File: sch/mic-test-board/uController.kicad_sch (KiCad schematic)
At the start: 3 parts, among them U34 SN74LVC126ARGYR, U5 NUCLEO144-H743ZI

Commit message: pcb: commit before large routing effort
 - schematic refactor to split preamps to each mic board
 - Mic board and main board are placed
 - no tracks laid
 - critical parts selected
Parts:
- added J1: CN11.female, ~, symbol Connector_Generic:Conn_02x35_Odd_Even
- added J5: CN12.female, ~, symbol Connector_Generic:Conn_02x35_Odd_Even
- added J6: CN11.male, ~, symbol Connector_Generic:Conn_02x35_Odd_Even
- added JP10, JP11, JP12, JP13, JP14, JP15, JP16, JP17, JP20, JP21, JP3, JP4, JP5, JP6, JP7, JP8, JP9: SolderJumper_2_Bridged, Jumper:SolderJumper-2_P1.3mm_Bridged_Pad1.0x1.5mm, symbol Jumper:SolderJumper_2_Bridged
- added R118, R119, R120: 0R, Resistor_SMD:R_0603_1608Metric, symbol Device:R_Small
- added R50, R52: 49.9k, Resistor_SMD:R_0603_1608Metric, symbol Device:R_Small
- added TP23, TP24, TP25, TP26, TP27, TP28, TP29, TP30, TP31, TP32, TP33, TP34, TP35: TestPoint, TestPoint:TestPoint_Pad_D1.0mm, symbol Connector:TestPoint
- C201: footprint (none) -> Capacitor_SMD:C_0603_1608Metric
- U5: footprint Module:ST_Morpho_Connector_144_STLink -> mic-test-board:ST_Morpho_Connector_144_STLink_SMD_Headers_BottomMount
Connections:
- net +3.3V: now also JP11.1 (A), JP12.1 (A), R50.2, R52.2
- net GND: now also U34.13
- net GPIO_DRDY: now also U5.140 (PG5), JP13.1 (A), TP27.1; no longer U34.1
- net GPIO_~{START}: now also JP14.1 (A), TP30.1
- net SPI1_MISO: now also JP21.1 (A), TP35.1
- net SPI1_MOSI: now also JP20.1 (A), TP34.1
- net SPI1_SCLK: now also JP17.1 (A), TP33.1
- net SPI1_~{CS1}: now also JP15.1 (A), TP31.1
- net SPI1_~{CS2}: now also JP16.1 (A), TP32.1
- net SPI2_MOSI1: now also TP28.1
- net SPI2_MOSI2: now also TP29.1
- net SPI2_SCLK: now also TP26.1
- net V_{IN}: now also U5.24 (VIN)
- net at U34.4: now also JP11.2 (B)
- net at U34.6: now also R119.1, TP24.1
- net SPI2_SCLK_buff: now reaches U5.114 (PF10)
- net SPI2_SCLK_buff: now also R118.2
- net GPIO_~{START}_uC: now reaches U5.141 (PG4)
- net GPIO_~{START}_uC: now also JP14.2 (B)
- net SPI1_~{CS1}_uC: now reaches U5.32 (PA4)
- net SPI1_~{CS1}_uC: now also JP15.2 (B)
- net LED5_uC: now reaches U5.39 (PD4)
- net LED5_uC: now also JP7.1 (A)
- net LED3_uC: now reaches U5.4 (PD2)
- net LED3_uC: now also JP5.1 (A)
- net LED4_uC: now reaches U5.40 (PD3)
- net LED4_uC: now also JP6.1 (A)
- net LED6_uC: now reaches U5.41 (PD5)
- net LED6_uC: now also JP8.1 (A)
- net LED7_uC: now reaches U5.43 (PD6)
- net LED7_uC: now also JP9.1 (A)
- net SPI1_MOSI_uC: now reaches U5.45 (PD7)
- net SPI1_MOSI_uC: now also JP20.2 (B)
- net SPI2_MOSI1_buff: now reaches U5.54 (PF8)
- net SPI2_MOSI1_buff: now also R119.2
- net LED2_uC: now reaches U5.55 (PD1)
- net LED2_uC: now also JP4.1 (A)
- net SPI2_MOSI2_buff: now reaches U5.56 (PF9)
- net SPI2_MOSI2_buff: now also R120.2
- net LED1_uC: now reaches U5.57 (PD0)
- net LED1_uC: now also JP3.1 (A)
- net LED8_uC: now reaches U5.63 (PG9)
- net LED8_uC: now also JP10.1 (A)
- net SPI1_~{CS2}_uC: now reaches U5.66 (PG10)
- net SPI1_~{CS2}_uC: now also JP16.2 (B)
- net SPI1_SCLK_uC: now reaches U5.83 (PA5)
- net SPI1_SCLK_uC: now also JP17.2 (B)
- net SPI1_MISO_uC: now reaches U5.85 (PA6)
- net SPI1_MISO_uC: now also JP21.2 (B)
- net ~{PButton2}: now reaches U5.94 (PB2)
- net ~{PButton2}: now also R52.1
- net ~{PButton1}: now reaches U5.96 (PB1)
- net ~{PButton1}: now also R50.1
- net at U34.10: now also JP12.2 (B)
- net at U34.8: now also R120.1, TP25.1
- net at U34.3: now also R118.1, TP23.1
- new net: JP13.2 (B), U34.1
- new net LED1: JP3.2 (B)
- new net LED2: JP4.2 (B)
- new net LED3: JP5.2 (B)
- new net LED4: JP6.2 (B)
- new net LED5: JP7.2 (B)
- new net LED6: JP8.2 (B)
- new net LED7: JP9.2 (B)
- new net LED8: JP10.2 (B)
- no-connect marks 4 -> 316
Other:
- note added: "72 way SMD headers: GEC36DFBN-M30 We only need 70-way, but the 70 ways are out of stock, or too expensive (eg: TSM-135-01-G-DV)"
- note added: "ADC Data Bus"
- note added: "Jumper on main page allows powering the Nucleo from external power supply. The Nucleo VIN pin feeds a LD1117S50TR LDO which can accept up to 15V, but has a 1.2V drop-out at 800mA. So, when powering from external source the minimum input voltage is: 6.2V"
- note added: "Nucleo Connectors"
- note added: "The 70-way male pins are way too expensive for how many pins we're actually using. So, just manully buy a few 8-ways and use them where needed"
- note added: "uController SPI1 bus is a master"
- note added: "uController SPI2 bus is a slave"
- note removed: "SPI1 bus is a master"
- note removed: "SPI2 bus is a slave"
- company: (none) -> Josh Berry
- title: (none) -> Sound Compass POC
- moved on the sheet: U34A, U34B, U34C, U34D

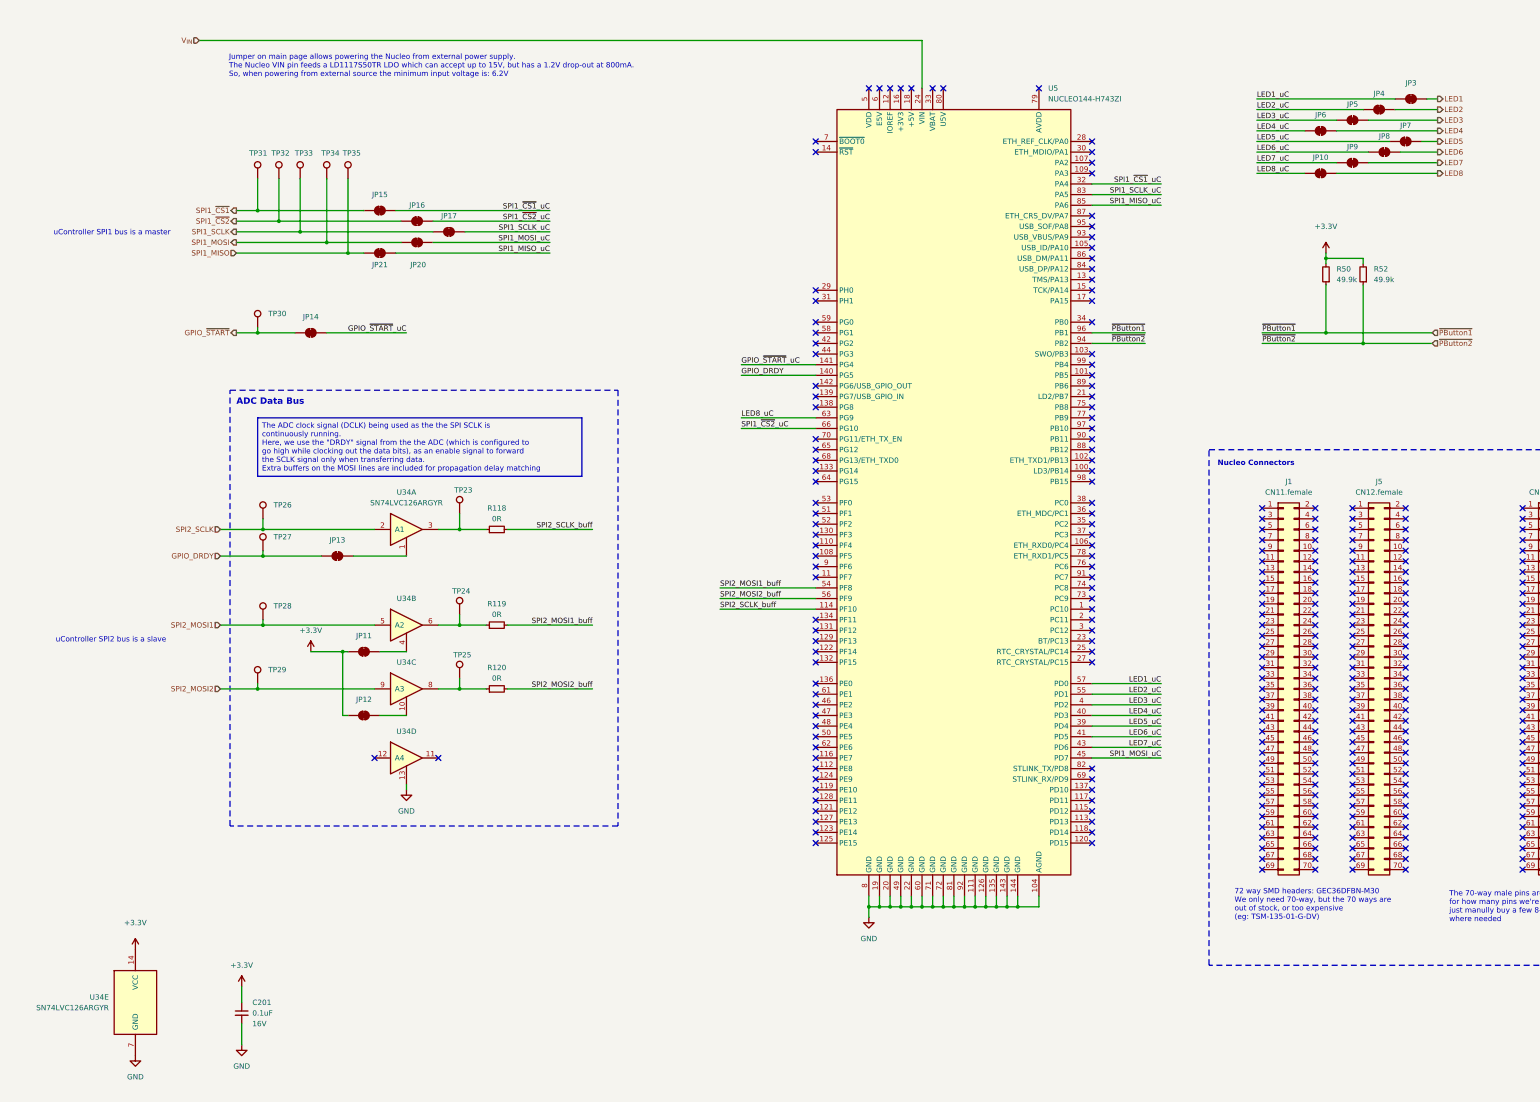
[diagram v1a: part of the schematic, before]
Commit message: pcb: finished routing mic board and ADC board.
 - BOM complete
 - uController pinout configured with CubeMX and re-checked
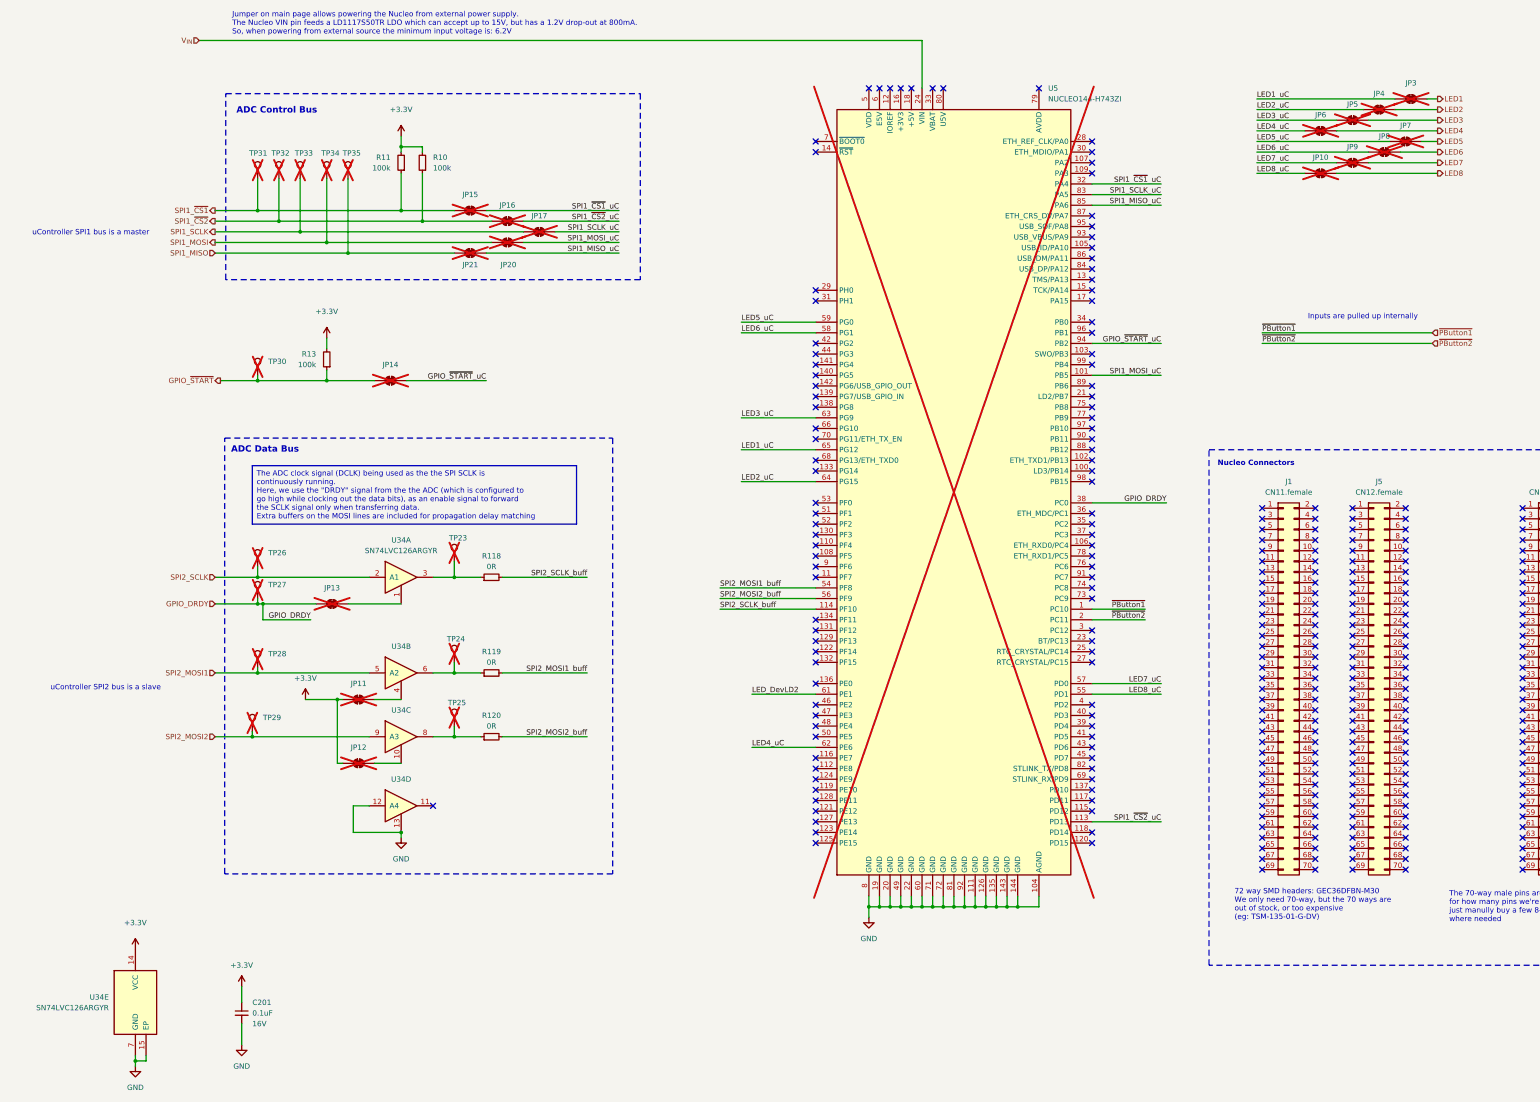
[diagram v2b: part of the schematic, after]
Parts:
- removed R50, R52: 49.9k, Resistor_SMD:R_0603_1608Metric, symbol Device:R_Small
- added R10, R11, R13: 100k, Resistor_SMD:R_0603_1608Metric, symbol Device:R_Small
- C201: Manufacturer (none) -> YAGEO; Part Number (none) -> CC0603KRX7R7BB104; Supplier (none) -> Digi-Key; Supplier Number (none) -> 311-1088-1-ND
- J1, J5, J6: Supplier (none) -> Digi-Key
- JP10, JP11, JP12, JP13, JP14, JP15, JP16, JP17, JP20, JP21, JP3, JP4, JP5, JP6, JP7, JP8, JP9, TP23, TP24, TP25, TP26, TP27, TP28, TP29, TP30, TP31, TP32, TP33, TP34, TP35, U5: now not fitted
- R118, R119, R120: Manufacturer (none) -> Stackpole Electronics Inc; Part Number (none) -> RMCF0603ZT0R00; Supplier (none) -> Digi-Key; Supplier Number (none) -> RMCF0603ZT0R00CT-ND
- U34: Manufacturer (none) -> Texas Instruments; Part Number (none) -> SN74LVC126ARGYR; Supplier (none) -> Digi-Key; Supplier Number (none) -> 296-13962-1-ND
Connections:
- net +3.3V: now also R10.2, R11.2, R13.2
- net GND: now also U34.12 (A4), U34.15 (EP)
- net GPIO_DRDY: now also U5.38 (PC0); no longer U5.140 (PG5)
- net GPIO_~{START}: now also R13.1
- net GPIO_~{START}_uC: now also U5.94 (PB2); no longer U5.141 (PG4)
- net LED1_uC: now also U5.65 (PG12); no longer U5.57 (PD0)
- net LED2_uC: now also U5.64 (PG15); no longer U5.55 (PD1)
- net LED3_uC: now also U5.63 (PG9); no longer U5.4 (PD2)
- net LED4_uC: now also U5.62 (PE6); no longer U5.40 (PD3)
- net LED5_uC: now also U5.59 (PG0); no longer U5.39 (PD4)
- net LED6_uC: now also U5.58 (PG1); no longer U5.41 (PD5)
- net LED7_uC: now also U5.57 (PD0); no longer U5.43 (PD6)
- net LED8_uC: now also U5.55 (PD1); no longer U5.63 (PG9)
- net SPI1_MOSI_uC: now also U5.101 (PB5); no longer U5.45 (PD7)
- net SPI1_~{CS1}: now also R11.1
- net SPI1_~{CS2}: now also R10.1
- net SPI1_~{CS2}_uC: now also U5.113 (PD13); no longer U5.66 (PG10)
- net ~{PButton1}: now also U5.1 (PC10); no longer U5.96 (PB1)
- net ~{PButton2}: now also U5.2 (PC11); no longer U5.94 (PB2)
- net LED_DevLD2: now reaches U5.61 (PE1)
- no-connect marks 316 -> 314
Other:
- note added: "ADC Control Bus"
- note added: "Inputs are pulled up internally"
- moved on the sheet: R118, R119, R120, U34A, U34B, U34C, U34D

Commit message: pcb: ordered PCB's and BOM! RevA and v240506
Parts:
- added J12: CN12.female, ~, symbol Connector_Generic:Conn_02x35_Odd_Even
- J1: value CN11.female -> CN11.male
- J5: value CN12.female -> CN12.male
- J6: value CN11.male -> CN11.female; Part Number PPTC042LFBN-RC -> PPPC362LFBN-RC; Supplier Number S7072-ND -> S7139-ND
- JP10, JP11, JP12, JP13, JP14, JP15, JP16, JP17, JP20, JP21, JP3, JP4, JP5, JP6, JP7, JP8, JP9: now fitted
- TP23, TP24, TP25, TP26, TP27, TP28, TP29, TP30, TP31, TP32, TP33, TP34, TP35, U5: now fitted; now left out of the parts list
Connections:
- no-connect marks 314 -> 384
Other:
- note added: "Populate female pins in the Nucleo, and male SMD header on this PCB"
- moved on the sheet: J1, J5
